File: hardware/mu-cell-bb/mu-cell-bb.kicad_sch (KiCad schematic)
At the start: 83 parts, among them IC1 SX1255IWLTRT, J1 TX, J2 RX, J3 EXT_CLK, J4 RPi GPIO, J5 IO, J6 TC2030, J7 TC2030, Q1 BC817-40W, Q2 BC817-40W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

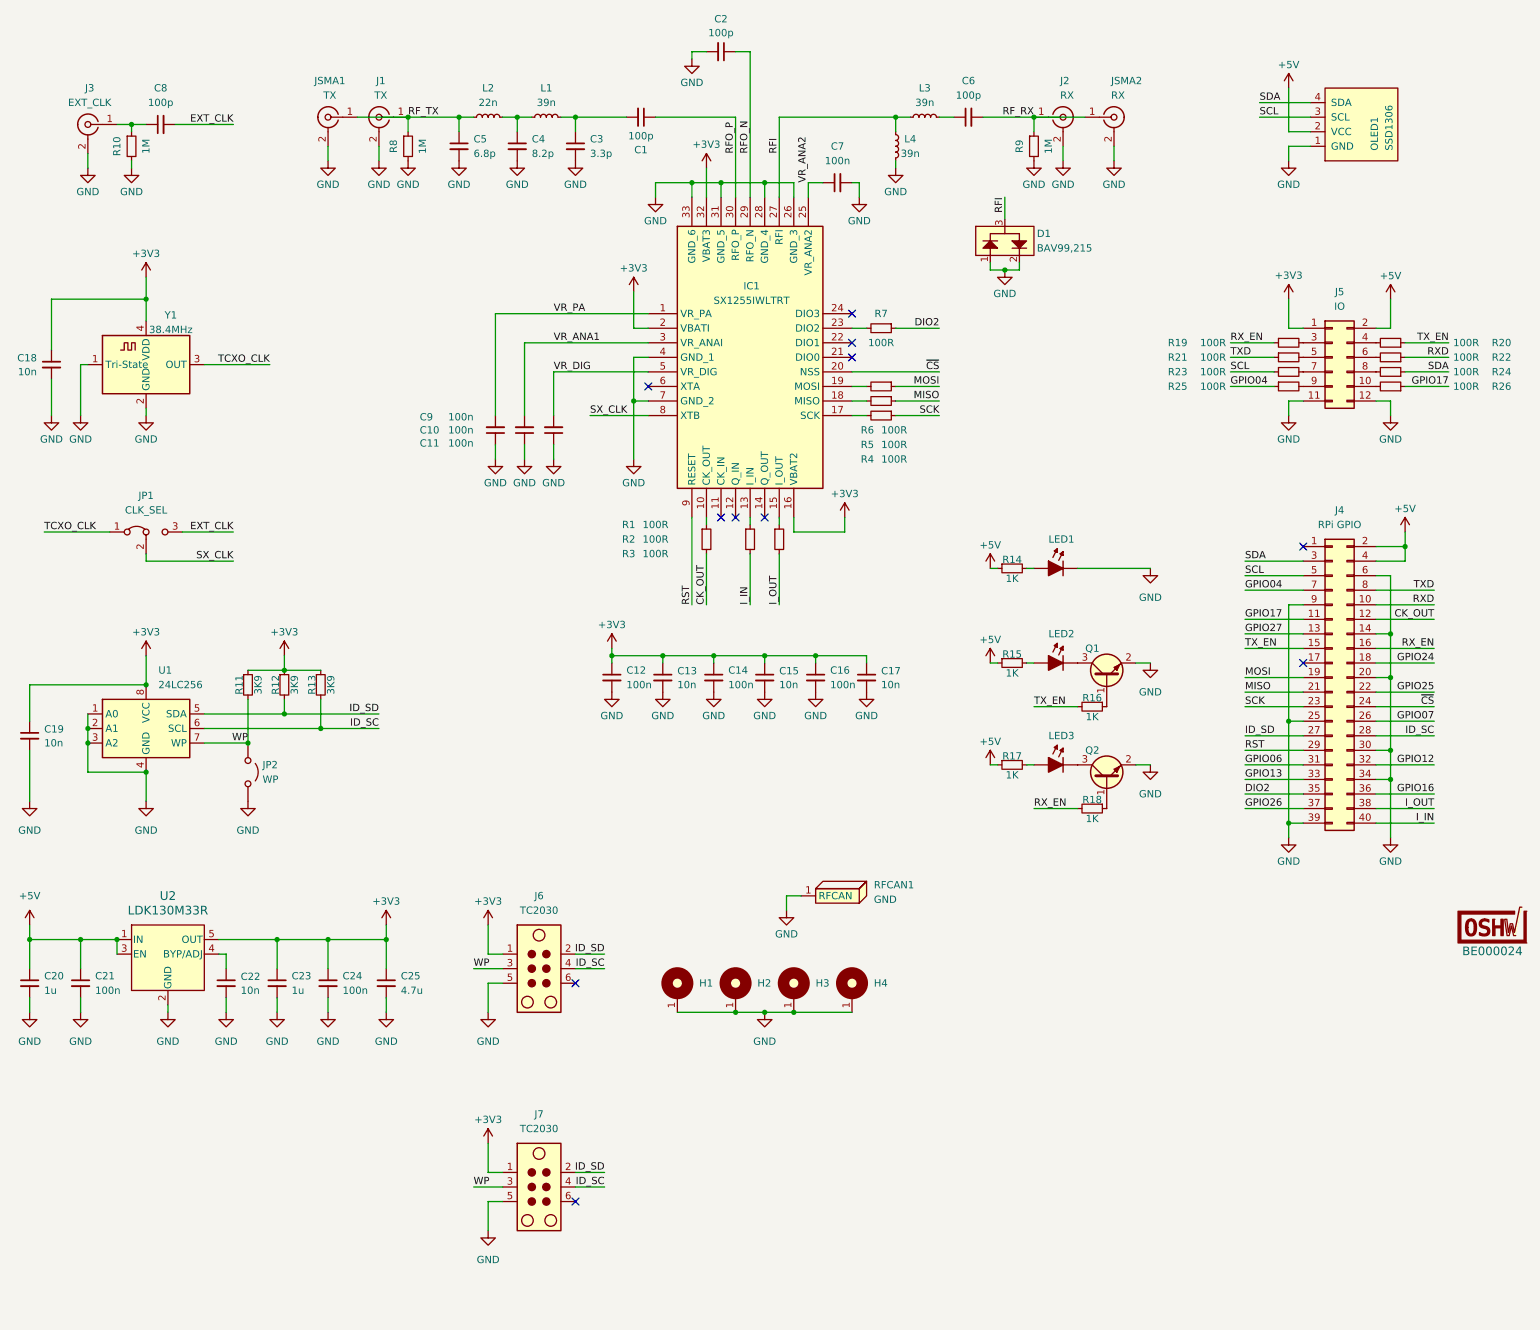
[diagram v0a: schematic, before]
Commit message: added muCell-BB v1.1 files
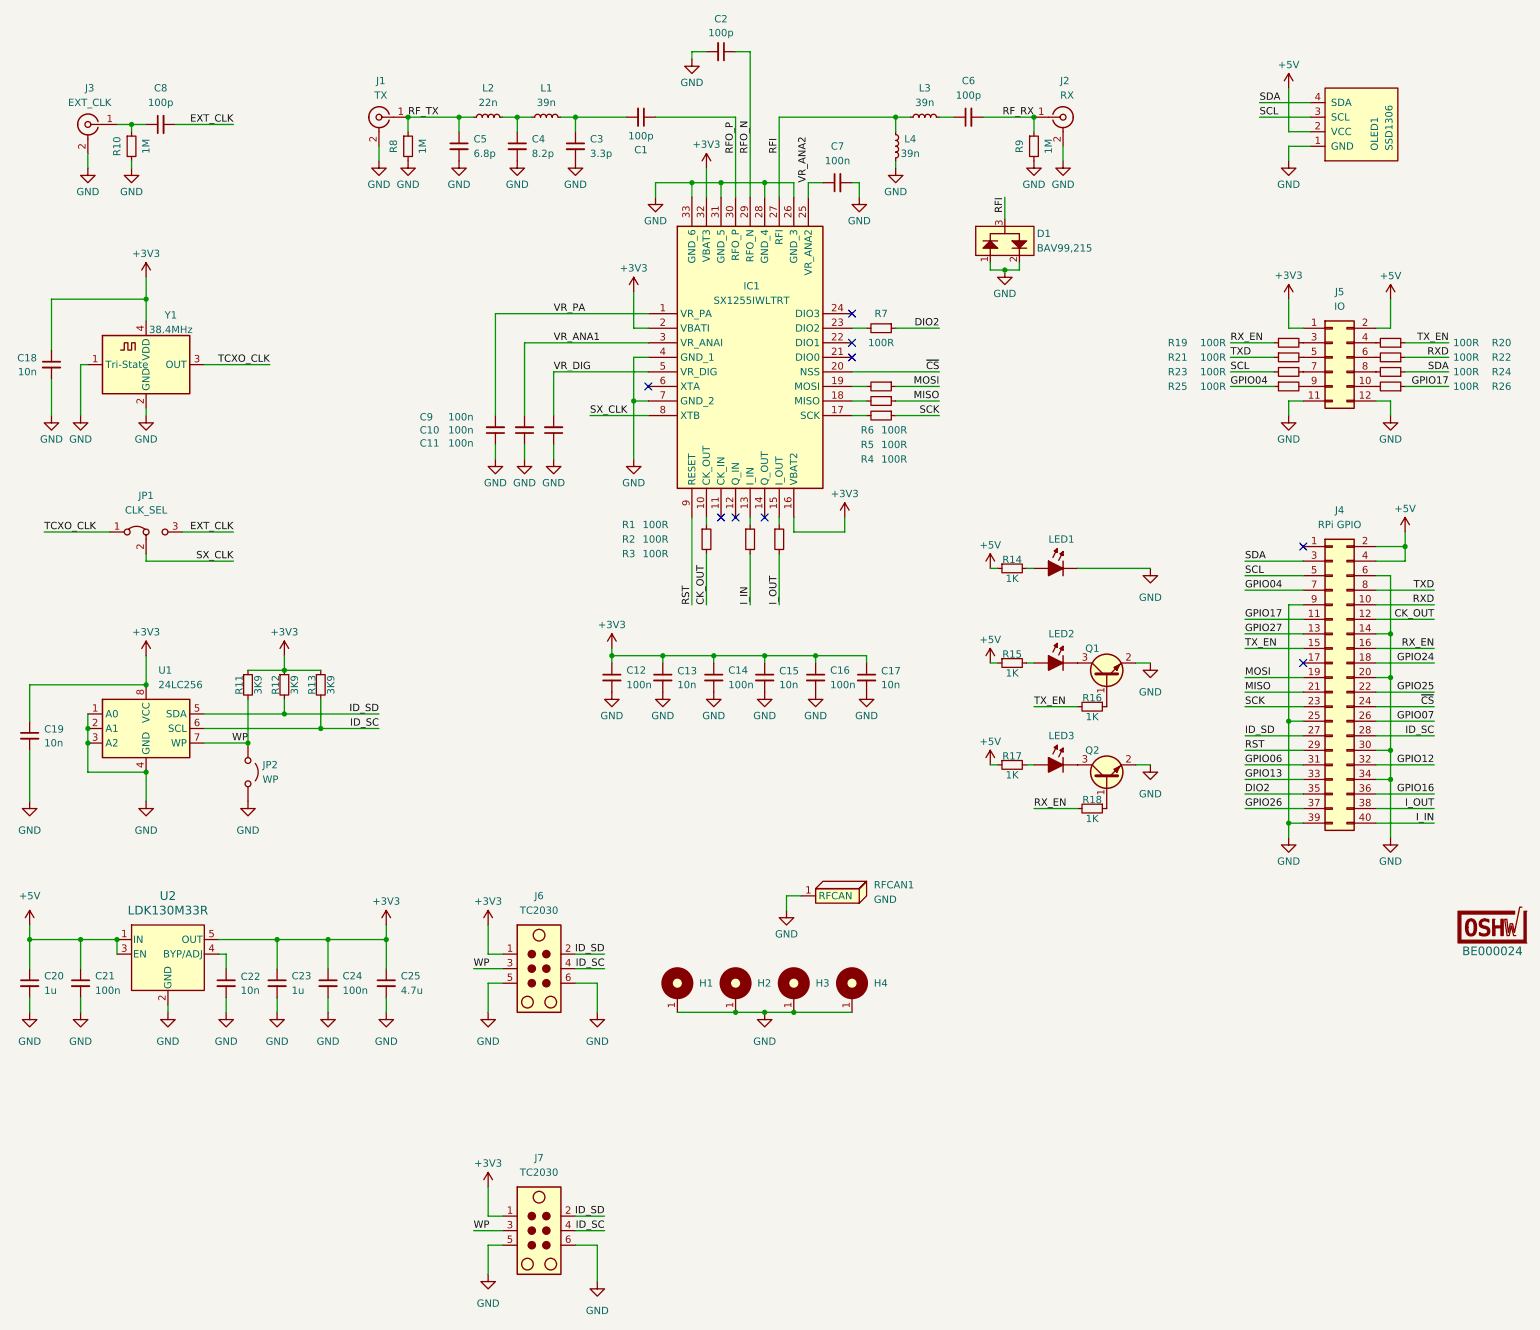
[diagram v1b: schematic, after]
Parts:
- removed JSMA1: TX, parts:BATWIRELESS_BWSMA-KE-P001, symbol parts:Conn_Coaxial
- removed JSMA2: RX, parts:BATWIRELESS_BWSMA-KE-P001, symbol parts:Conn_Coaxial
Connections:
- net GND: now also J6.6, J7.6
- no-connect marks 11 -> 9
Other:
- moved on the sheet: J7

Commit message: added v1.2 PCB files
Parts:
- RFCAN1: now left out of the parts list
- Y1: footprint parts:Oscillator_SMD_ECS_2520MV-xxx-xx-4Pin_2.5x2.0mm -> Crystal:Crystal_SMD_2016-4Pin_2.0x1.6mm
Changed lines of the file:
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@@
 	(title_block
 		(title "µCell - BB")
-		(date "2026-03-10")
-		(rev "v1.1")
+		(date "2026-05-24")
+		(rev "v1.2")
 		(company "jankyneering.cc")
 		(comment 1 "ON4PFD, ON6RF")
@@
 			)
 		)
-		(property "Footprint" "parts:Oscillator_SMD_ECS_2520MV-xxx-xx-4Pin_2.5x2.0mm"
+		(property "Footprint" "Crystal:Crystal_SMD_2016-4Pin_2.0x1.6mm"
 			(at 52.07 83.82 0)
 			(hide yes)
@@
 			)
 		)
-		(property "Datasheet" "https://www.ecsxtal.com/store/pdf/ECS-2520MV.pdf"
+		(property "Datasheet" "https://jlc-prod-smt.oss-eu-central-1.aliyuncs.com/smtDataManualFile/8589791319397724160-C1987359.pdf?response-content-disposition=attachment%3B%20filename%3DC1987359.pdf%3B%20filename%2A%3DUTF-8%27%27C1987359.pdf&x-oss-date=20260524T184223Z&x-oss-expires=1800&x-oss-security-token=CAISgAN1q6Ft5B2yfSjIr5veHPbQm6dv%2BaeRYGLhjTRiPdxBubHdlTz2IHhMdHJsAOodtv0%2FmmhT6PkclqRLcbhpcmfjV%2BZHzLB8qdRnhz9M4J7b16cNrbH4M4H6aXeirtuwDsz9SNTCALjPD3nPii50x5bjaDymRCbLGJaViJlhHLN1Ow6jdmhpCctxLAlvo9NgFxm3D%2Fu2NQPwiWf9FVdhvhEG6Vly8qOi2MaRmFy8yFTx0b0SvJ%2BjYMrmPctoN9JnSdC5mfdzau3a1TJ84gRD0a5wkaVA1zbDs5bfISEIuUzebreLqY03dV4mOvdqIcMe8qigz88fk%2FfIioH6xyxKOexoSCnFTOiiupCcQLPyao9jLu6iayqViY7QaIOTqQohZmkAMwVOasAsI3Ngh4zF97Qt0cVNkXO9gWfLI8DtuMleWiriQvdNMnSgc5lCkRRYwGs1287ugXlSQzo890KPDAEovaKCnZ2ZSfh7Y4sNknI6i%2Bfc2Se2MIkIrv12yqKWD5sagAE79bwWWUez5c%2FB4w2criuVba2OLz%2B02RFmm7CNYMmXf9fIxUIj1Twk5Pv7K8P8RkNlBHnj2loAVKu%2FB9is9vQ%2F3a%2BJscBcD20YJYXv%2FESbiukC8mBBsJqIAWMVF0nbhi%2FBqBihkwEhRlF6yWAlh3xdp%2B4uenRhDtFeiIWXE%2FxsoyAA&x-oss-signature-version=OSS4-HMAC-SHA256&x-oss-credential=STS.NXkWLdvxNNezbDPi471SmVtvw%2F20260524%2Feu-central-1%2Foss%2Faliyun_v4_request&x-oss-signature=063c7ceb01ce589fe3dfd7678514f4a9f9039a99d840c6cbbb7f39b023bcb9fd"
 			(at 36.195 71.755 0)
 			(hide yes)
@@
 			)
 		)
-		(property "Description" "HCMOS Crystal Clock Oscillator, 2.5x2.0 mm SMD"
+		(property "Description" "HCMOS Crystal Clock Oscillator, 2.0x1.6 mm SMD"
 			(at 40.64 74.93 0)
 			(hide yes)
@@
 		(body_style 1)
 		(exclude_from_sim no)
-		(in_bom yes)
-		(on_board yes)
-		(in_pos_files yes)
+		(in_bom no)
+		(on_board no)
+		(in_pos_files no)
 		(dnp no)
 		(fields_autoplaced yes)
